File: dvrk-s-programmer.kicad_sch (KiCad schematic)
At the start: 19 parts, among them J2 Conn_01x04, J3 Conn_02x05_Odd_Even, SW1 SW_SPDT, U1 STM32F103C8Tx, U3 XKTF-015-N

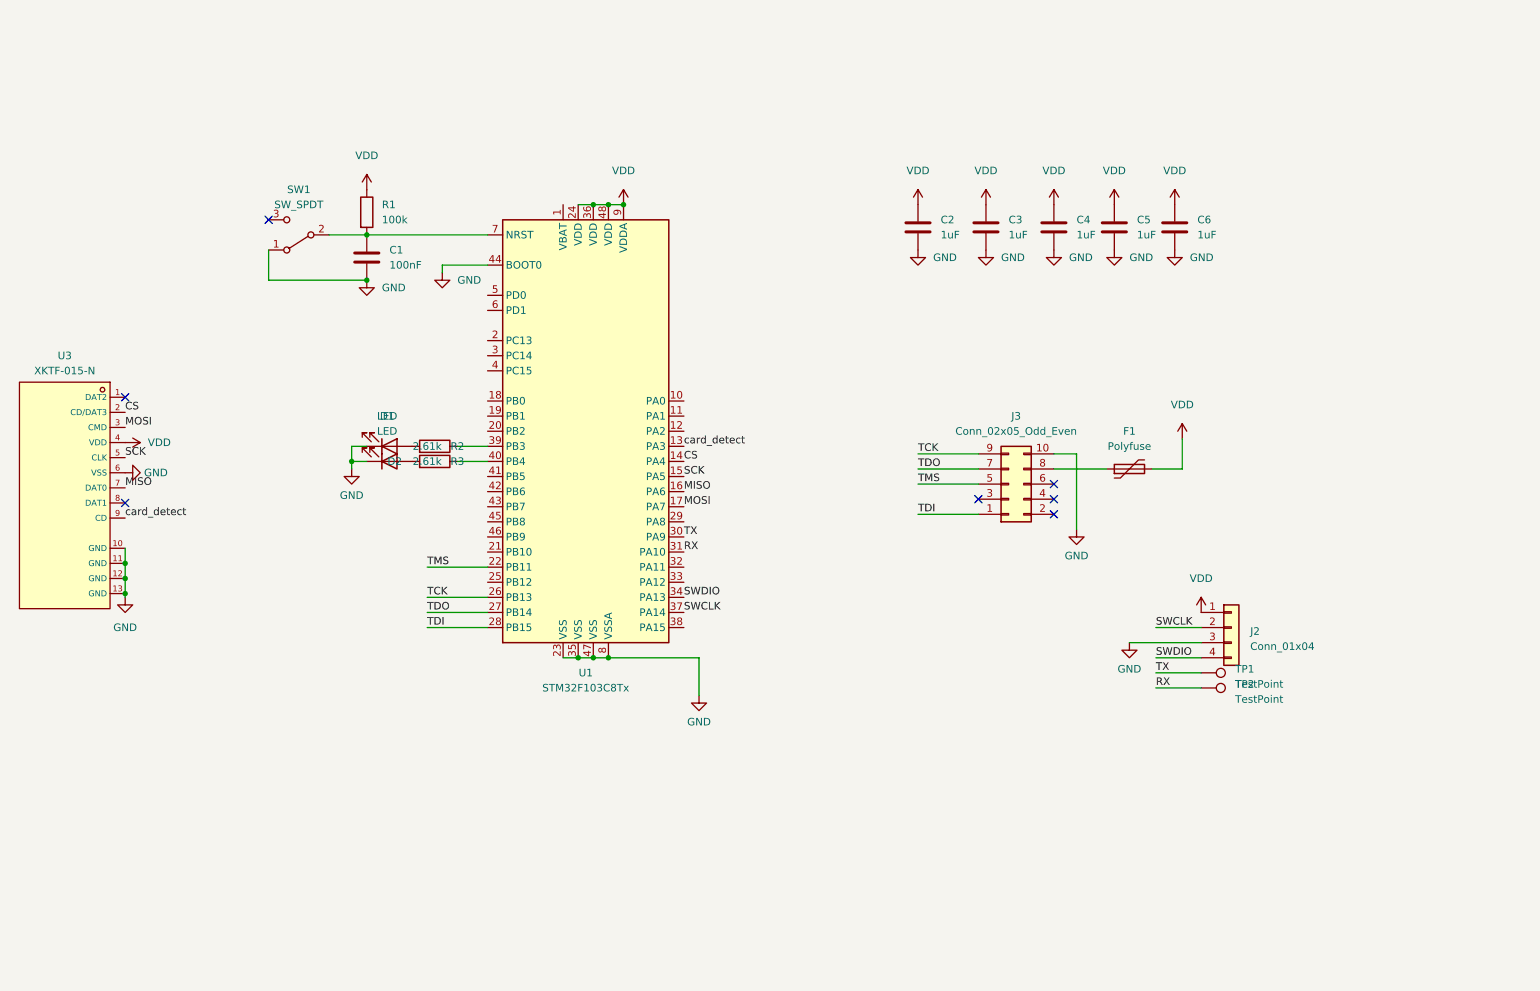
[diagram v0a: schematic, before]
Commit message: changed mcu. added usb.
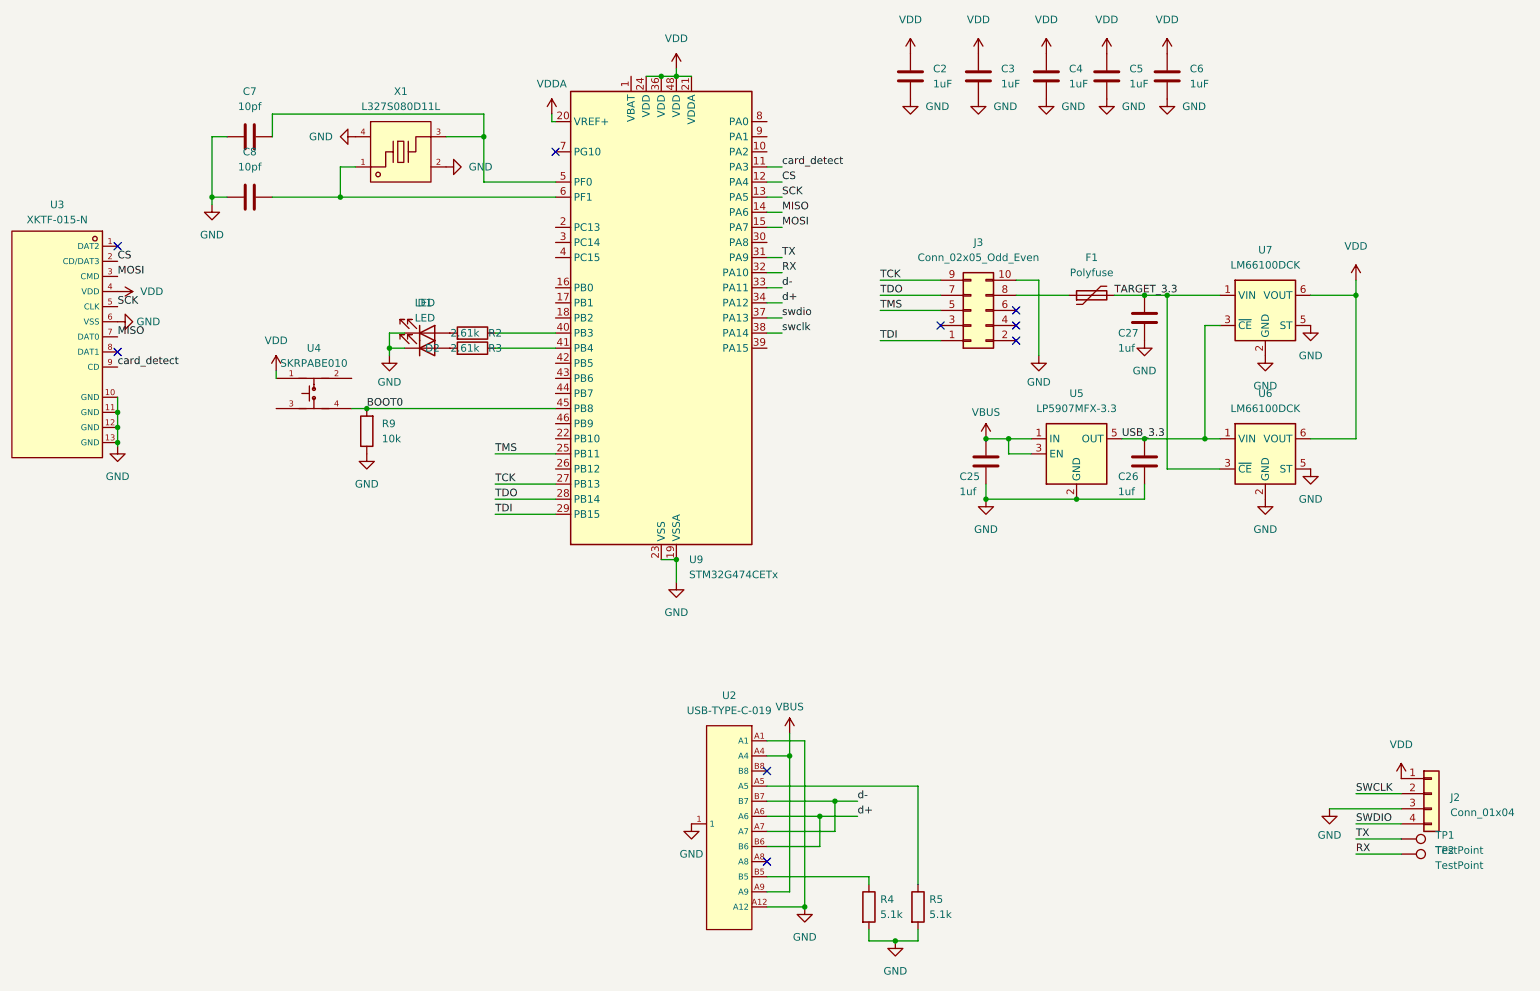
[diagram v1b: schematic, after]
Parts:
- removed C1: 100nF, Capacitor_SMD:C_0402_1005Metric, symbol Device:C
- removed R1: 100k, Resistor_SMD:R_0402_1005Metric, symbol Device:R
- removed SW1: SW_SPDT, Button_Switch_SMD:SW_SPDT_PCM12, symbol Switch:SW_SPDT
- removed U1: STM32F103C8Tx, Package_QFP:LQFP-48_7x7mm_P0.5mm, symbol MCU_ST_STM32F1:STM32F103C8Tx
- added C25, C26, C27: 1uf, Capacitor_SMD:C_0402_1005Metric, symbol Device:C
- added C7, C8: 10pf, Capacitor_SMD:C_0402_1005Metric, symbol Device:C
- added R4, R5: 5.1k, Resistor_SMD:R_0402_1005Metric, symbol Device:R
- added R9: 10k, Resistor_SMD:R_0402_1005Metric, symbol Device:R
- added U2: USB-TYPE-C-019, footprint:TYPE-C-SMD_HX-TYPE-C-16PIN, symbol jlc_kicad_lib:USB-TYPE-C-019
- added U4: SKRPABE010, footprint:KEY-SMD_4P-L4.2-W3.2-P2.20-LS4.6, symbol jlc2:SKRPABE010
- added U5: LP5907MFX-3.3, Package_TO_SOT_SMD:SOT-23-5, symbol Regulator_Linear:LP5907MFX-3.3
- added U6, U7: LM66100DCK, Package_TO_SOT_SMD:SOT-363_SC-70-6, symbol Power_Management:LM66100DCK
- added U9: STM32G474CETx, Package_QFP:LQFP-48_7x7mm_P0.5mm, symbol MCU_ST_STM32G4:STM32G474CETx
- added X1: L327S080D11L, footprint:CRYSTAL-SMD_4P-L3.2-W2.5-BL, symbol jlc2:L327S080D11L
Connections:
- net CS: now also U9.12 (PA4)
- net GND: now also C25.1, C26.1, C27.1, C7.1, C8.1, R4.2, R5.2, R9.1, U2.1, U2.A1, U2.A12, U5.2 (GND), U6.2 (GND), U6.5 (ST), U7.2 (GND), U7.5 (ST), U9.19 (VSSA), U9.23 (VSS), U9.35 (VSS), U9.47 (VSS), X1.2 (GND), X1.4 (GND)
- net MISO: now also U9.14 (PA6)
- net MOSI: now also U9.15 (PA7)
- net RX: now also U9.32 (PA10)
- net SCK: now also U9.13 (PA5)
- net TCK: now also U9.27 (PB13)
- net TDI: now also U9.29 (PB15)
- net TDO: now also U9.28 (PB14)
- net TMS: now also U9.25 (PB11)
- net TX: now also U9.31 (PA9)
- net VDD: now also U4.1, U6.6 (VOUT), U7.6 (VOUT), U9.21 (VDDA), U9.24 (VDD), U9.36 (VDD), U9.48 (VDD); no longer F1.2
- net card_detect: now also U9.11 (PA3)
- net at R3.1: now also U9.40 (PB3)
- net at R2.1: now also U9.41 (PB4)
- new net: R4.1, U2.B5
- new net: R5.1, U2.A5
- new net: C8.2, U9.6 (PF1), X1.1
- new net: C7.2, U9.5 (PF0), X1.3
- new net BOOT0: R9.2, U4.4, U9.45 (PB8)
- new net TARGET_3.3: C27.2, F1.2, U6.3 (~{CE}), U7.1 (VIN)
- new net USB_3.3: C26.2, U5.5 (OUT), U6.1 (VIN), U7.3 (~{CE})
- new net VBUS: C25.2, U2.A4, U2.A9, U5.1 (IN), U5.3 (EN)
- new net VDDA: U9.20 (VREF+)
- new net d+: U2.A6, U2.B6, U9.34 (PA12)
- new net d-: U2.A7, U2.B7, U9.33 (PA11)
- new net swclk: U9.38 (PA14)
- new net swdio: U9.37 (PA13)
- no-connect marks 7 -> 9
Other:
- moved on the sheet: C2, C3, C4, C5, C6, D1, D2, F1, J2, J3, R2, R3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

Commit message: added led array. changed microcontroller.
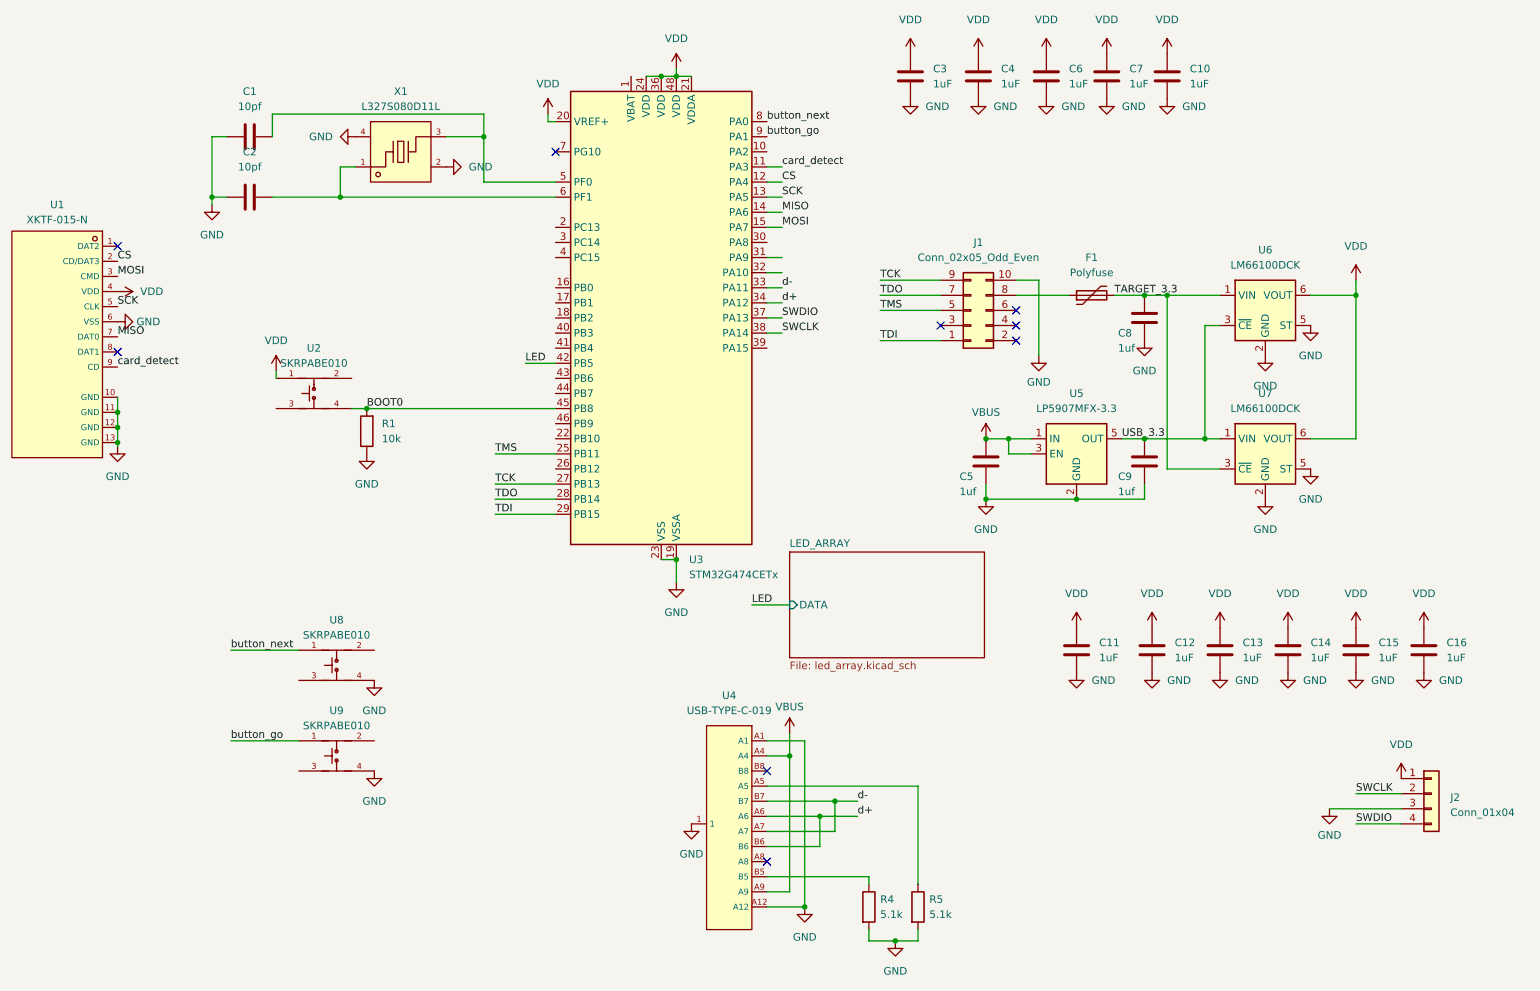
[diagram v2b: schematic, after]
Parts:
- removed D1, D2: LED, LED_SMD:LED_0603_1608Metric, symbol Device:LED
- removed R2, R3: 2.61k, Resistor_SMD:R_0402_1005Metric, symbol Device:R
- removed TP1, TP2: TestPoint, TestPoint:TestPoint_Pad_1.0x1.0mm, symbol Connector:TestPoint
- added C11, C12, C13, C14, C15, C16: 1uF, Capacitor_SMD:C_0402_1005Metric, symbol Device:C
- added U8, U9: SKRPABE010, footprint:KEY-SMD_4P-L4.2-W3.2-P2.20-LS4.6, symbol jlc2:SKRPABE010
- renumbered C7 to C1, C6 to C10, C8 to C2, C2 to C3, C3 to C4, C25 to C5, C4 to C6, C5 to C7, C27 to C8, C26 to C9, J3 to J1, R9 to R1, U3 to U1, U4 to U2, U9 to U3, U2 to U4, U7 to U6, U6 to U7
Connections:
- net VDDA is gone; now on net VDD: U3.20 (VREF+)
- net swclk is gone; now on net SWCLK: U3.38 (PA14)
- net swdio is gone; now on net SWDIO: U3.37 (PA13)
- net GND: now also C11.2, C12.2, C13.2, C14.2, C15.2, C16.2, U8.4, U9.4
- net VDD: now also C11.1, C12.1, C13.1, C14.1, C15.1, C16.1
- net LED: now reaches U3.42 (PB5)
- net button_next: now reaches U3.8 (PA0)
- net button_next: now also U8.1
- net button_go: now reaches U3.9 (PA1)
- net button_go: now also U9.1
- net RX: no longer names the net of U3.32 (PA10)
- net TX: no longer names the net of U3.31 (PA9)
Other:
- added sheet LED_ARRAY (led_array.kicad_sch)
